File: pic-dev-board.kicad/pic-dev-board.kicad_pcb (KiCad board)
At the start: 2 copper layers, 100 x 100 mm, 78 parts, among them J1 Conn_GP0, J10 Jumper DATin, J11 Conn_SR_2, J12 Conn_SR_1, J13 Conn_5V_GND, J14 Jumper CLKin, J15 Barrel_Jack_Switch, J16 RUN/~PGM, J17 I2C, J18 GP1(RA1)/RB6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

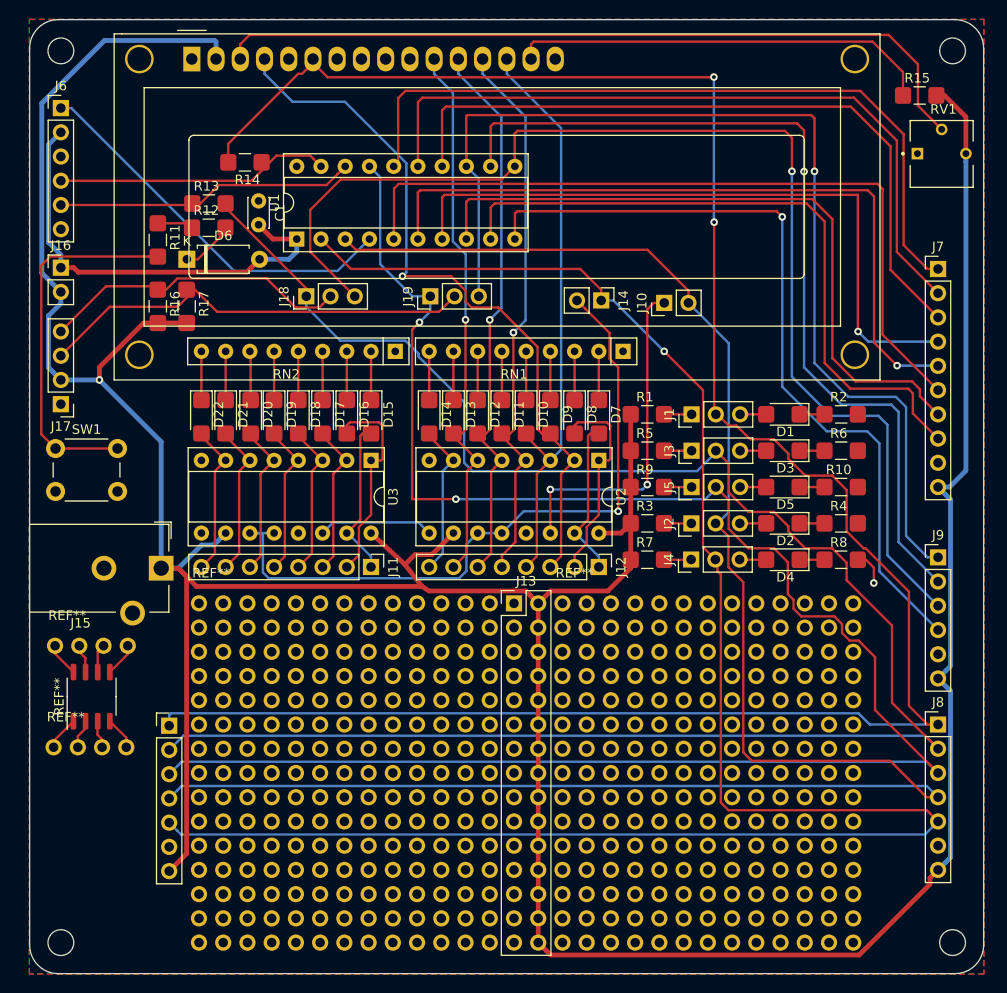
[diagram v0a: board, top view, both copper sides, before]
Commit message: added labels
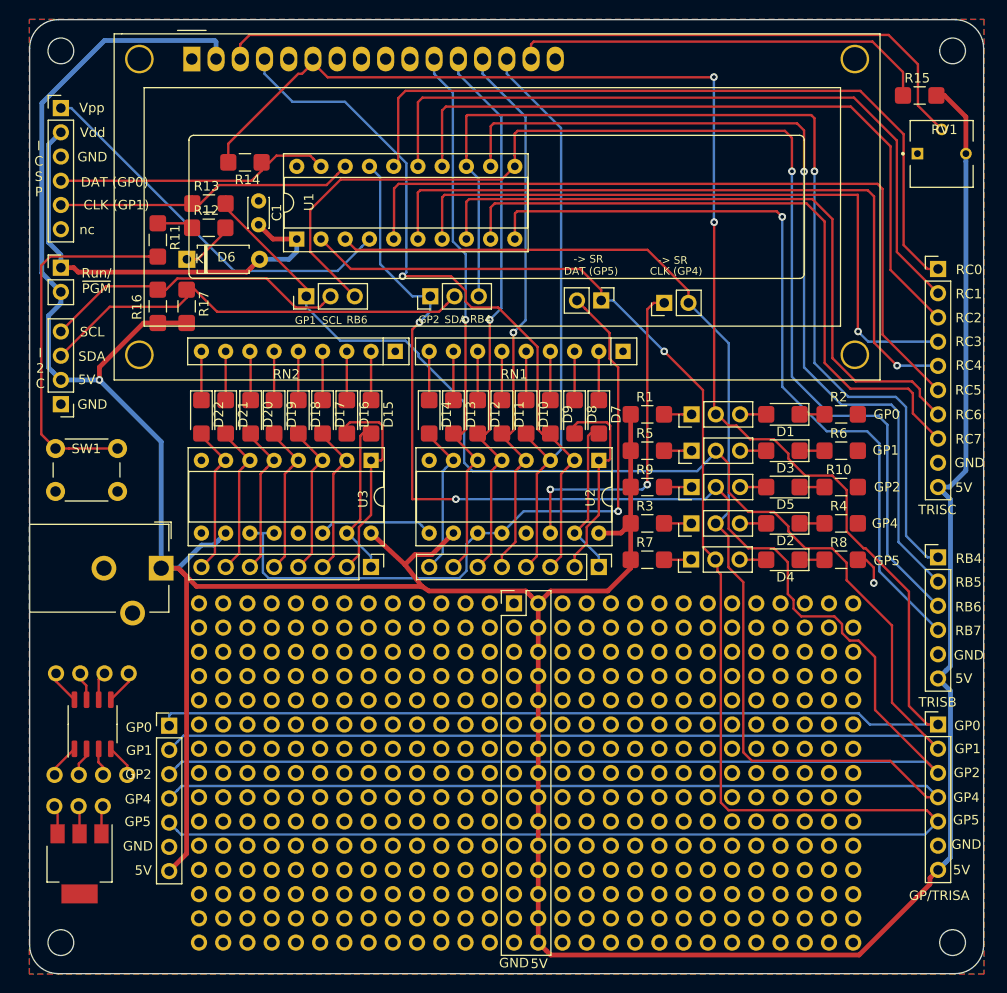
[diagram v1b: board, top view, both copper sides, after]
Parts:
- removed the REF** at (32.5, 106.3)
- removed the REF** at (32.7, 95.6)
- added REF**: Proto_Area_03x01_P2.54mm_Drill1.0mm, Proto_Area:Proto_Area_03x01, F.Cu at (37.7, 112.4)
- added REF**: SOT-223, Package_TO_SOT_SMD:SOT-223, F.Cu at (35.2, 118.5)
- added REF**: Proto_Area_04x01_P2.54mm_Drill1.0mm, Proto_Area:Proto_Area_04x01, F.Cu at (32.6, 109.2)
- added REF**: Proto_Area_04x01_P2.54mm_Drill1.0mm, Proto_Area:Proto_Area_04x01, F.Cu at (32.8, 98.5)
- moved REF** 2.90 mm to (36.6, 103.9)
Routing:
- net (no net): track 26.2 -> 35.1 mm
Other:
- board text added: "-> SR"
- board text added: "5V"
- board text added: "CLK (GP1)"
- board text added: "CLK (GP4)"
- board text added: "DAT (GP0)"
- board text added: "DAT (GP5)"
- board text added: "GND"
- board text added: "GP/TRISA"
- board text added: "GP0"
- board text added: "GP1"
- board text added: "GP2"
- board text added: "GP4"
- board text added: "GP5"
- board text added: "I 2 C"
- board text added: "I C S P"
- board text added: "RB4"
- board text added: "RB5"
- board text added: "RB6"
- board text added: "RB7"
- board text added: "RC0"
- board text added: "RC1"
- board text added: "RC2"
- board text added: "RC3"
- board text added: "RC4"
- board text added: "RC5"
- board text added: "RC6"
- board text added: "RC7"
- board text added: "Run/ ~PGM"
- board text added: "SCL"
- board text added: "SDA"
- board text added: "TRISB"
- board text added: "TRISC"
- board text added: "Vdd"
- board text added: "Vpp"
- board text added: "nc"

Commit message: Rev1: updated date/revision and added label
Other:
- board text added: "Rev 1"
- board text added: "https://github.com/bablokb/pcb-pic-devboard"
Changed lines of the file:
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@@
   (general
     (thickness 1.6)
-    (drawings 71)
+    (drawings 73)
     (tracks 699)
     (zones 0)
@@
     )
   )
+  (gr_text "Rev 1" (at 112.4458 39.9796) (layer B.SilkS)
+    (effects (font (size 1 1) (thickness 0.15)) (justify mirror))
+  )
+  (gr_text https://github.com/bablokb/pcb-pic-devboard (at 96.2152 38.3286) (layer B.SilkS)
+    (effects (font (size 1 1) (thickness 0.15)) (justify mirror))
+  )
   (gr_text GP4 (at 119.6594 82.804) (layer F.SilkS)
     (effects (font (size 1 1) (thickness 0.15)))
@@
   )
   (gr_text 5V (at 127.9144 79.0448) (layer F.SilkS)
-    (effects (font (size 1 1) (thickness 0.15)))
+    (effects (font (size 1 0.8) (thickness 0.15)))
   )
-  (gr_text GND (at 128.524 76.454) (layer F.SilkS)
-    (effects (font (size 1 1) (thickness 0.15)))
+  (gr_text GND (at 128.2954 76.4286) (layer F.SilkS)
+    (effects (font (size 1 0.8) (thickness 0.15)))
   )
-  (gr_text RC7 (at 128.4224 73.9648) (layer F.SilkS)
-    (effects (font (size 1 1) (thickness 0.15)))
+  (gr_text RC7 (at 128.1938 73.9394) (layer F.SilkS)
+    (effects (font (size 1 0.8) (thickness 0.15)))
   )
-  (gr_text RC6 (at 128.4224 71.4248) (layer F.SilkS)
-    (effects (font (size 1 1) (thickness 0.15)))
+  (gr_text RC6 (at 128.1938 71.3994) (layer F.SilkS)
+    (effects (font (size 1 0.8) (thickness 0.15)))
   )
-  (gr_text RC5 (at 128.397 68.834) (layer F.SilkS)
-    (effects (font (size 1 1) (thickness 0.15)))
+  (gr_text RC5 (at 128.1684 68.8086) (layer F.SilkS)
+    (effects (font (size 1 0.8) (thickness 0.15)))
   )
-  (gr_text RC4 (at 128.4478 66.2432) (layer F.SilkS)
-    (effects (font (size 1 1) (thickness 0.15)))
+  (gr_text RC4 (at 128.2192 66.2178) (layer F.SilkS)
+    (effects (font (size 1 0.8) (thickness 0.15)))
   )
-  (gr_text RC3 (at 128.4224 63.754) (layer F.SilkS)
-    (effects (font (size 1 1) (thickness 0.15)))
+  (gr_text RC3 (at 128.1938 63.7286) (layer F.SilkS)
+    (effects (font (size 1 0.8) (thickness 0.15)))
   )
-  (gr_text RC2 (at 128.4224 61.2648) (layer F.SilkS)
-    (effects (font (size 1 1) (thickness 0.15)))
+  (gr_text RC2 (at 128.1938 61.2394) (layer F.SilkS)
+    (effects (font (size 1 0.8) (thickness 0.15)))
   )
-  (gr_text RC1 (at 128.4478 58.7502) (layer F.SilkS)
-    (effects (font (size 1 1) (thickness 0.15)))
+  (gr_text RC1 (at 128.2192 58.7248) (layer F.SilkS)
+    (effects (font (size 1 0.8) (thickness 0.15)))
   )
-  (gr_text RC0 (at 128.4732 56.2102) (layer F.SilkS)
-    (effects (font (size 1 1) (thickness 0.15)))
+  (gr_text RC0 (at 128.2446 56.1848) (layer F.SilkS)
+    (effects (font (size 1 0.8) (thickness 0.15)))
   )
-  (gr_text 5V (at 127.9144 99.06) (layer F.SilkS)
-    (effects (font (size 1 1) (thickness 0.15)))
+  (gr_text 5V (at 127.7874 99.0346) (layer F.SilkS)
+    (effects (font (size 1 0.8) (thickness 0.15)))
   )
-  (gr_text GND (at 128.4478 96.6216) (layer F.SilkS)
-    (effects (font (size 1 1) (thickness 0.15)))
+  (gr_text GND (at 128.3208 96.5962) (layer F.SilkS)
+    (effects (font (size 1 0.8) (thickness 0.15)))
   )
-  (gr_text RB7 (at 128.397 94.0562) (layer F.SilkS)
-    (effects (font (size 1 1) (thickness 0.15)))
+  (gr_text RB7 (at 128.27 94.0308) (layer F.SilkS)
+    (effects (font (size 1 0.8) (thickness 0.15)))
   )
-  (gr_text RB6 (at 128.397 91.567) (layer F.SilkS)
-    (effects (font (size 1 1) (thickness 0.15)))
+  (gr_text RB6 (at 128.27 91.5416) (layer F.SilkS)
+    (effects (font (size 1 0.8) (thickness 0.15)))
   )
-  (gr_text RB5 (at 128.4224 88.9762) (layer F.SilkS)
-    (effects (font (size 1 1) (thickness 0.15)))
+  (gr_text RB5 (at 128.2954 88.9508) (layer F.SilkS)
+    (effects (font (size 1 0.8) (thickness 0.15)))
   )
-  (gr_text RB4 (at 128.4478 86.487) (layer F.SilkS)
-    (effects (font (size 1 1) (thickness 0.15)))
+  (gr_text RB4 (at 128.3208 86.4616) (layer F.SilkS)
+    (effects (font (size 1 0.8) (thickness 0.15)))
   )
   (gr_text TRISC (at 125.1458 81.3816) (layer F.SilkS)
@@
   )
   (gr_text 5V (at 127.6858 119.126) (layer F.SilkS)
-    (effects (font (size 1 1) (thickness 0.15)))
+    (effects (font (size 1 0.8) (thickness 0.15)))
   )
   (gr_text GP1 (at 128.3208 106.426) (layer F.SilkS)
-    (effects (font (size 1 1) (thickness 0.15)))
+    (effects (font (size 1 0.8) (thickness 0.15)))
   )
   (gr_text GP2 (at 128.2446 108.9406) (layer F.SilkS)
-    (effects (font (size 1 1) (thickness 0.15)))
+    (effects (font (size 1 0.8) (thickness 0.15)))
   )
   (gr_text GP5 (at 128.1684 113.8936) (layer F.SilkS)
-    (effects (font (size 1 1) (thickness 0.15)))
+    (effects (font (size 1 0.8) (thickness 0.15)))
   )
   (gr_text GP0 (at 128.2954 104.013) (layer F.SilkS)
-    (effects (font (size 1 1) (thickness 0.15)))
+    (effects (font (size 1 0.8) (thickness 0.15)))
   )
   (gr_text GND (at 128.1938 116.459) (layer F.SilkS)
-    (effects (font (size 1 1) (thickness 0.15)))
+    (effects (font (size 1 0.8) (thickness 0.15)))
   )
   (gr_text GP4 (at 128.1938 111.5314) (layer F.SilkS)
-    (effects (font (size 1 1) (thickness 0.15)))
+    (effects (font (size 1 0.8) (thickness 0.15)))
   )
   (gr_text 5V (at 83.4136 128.9558) (layer F.SilkS)

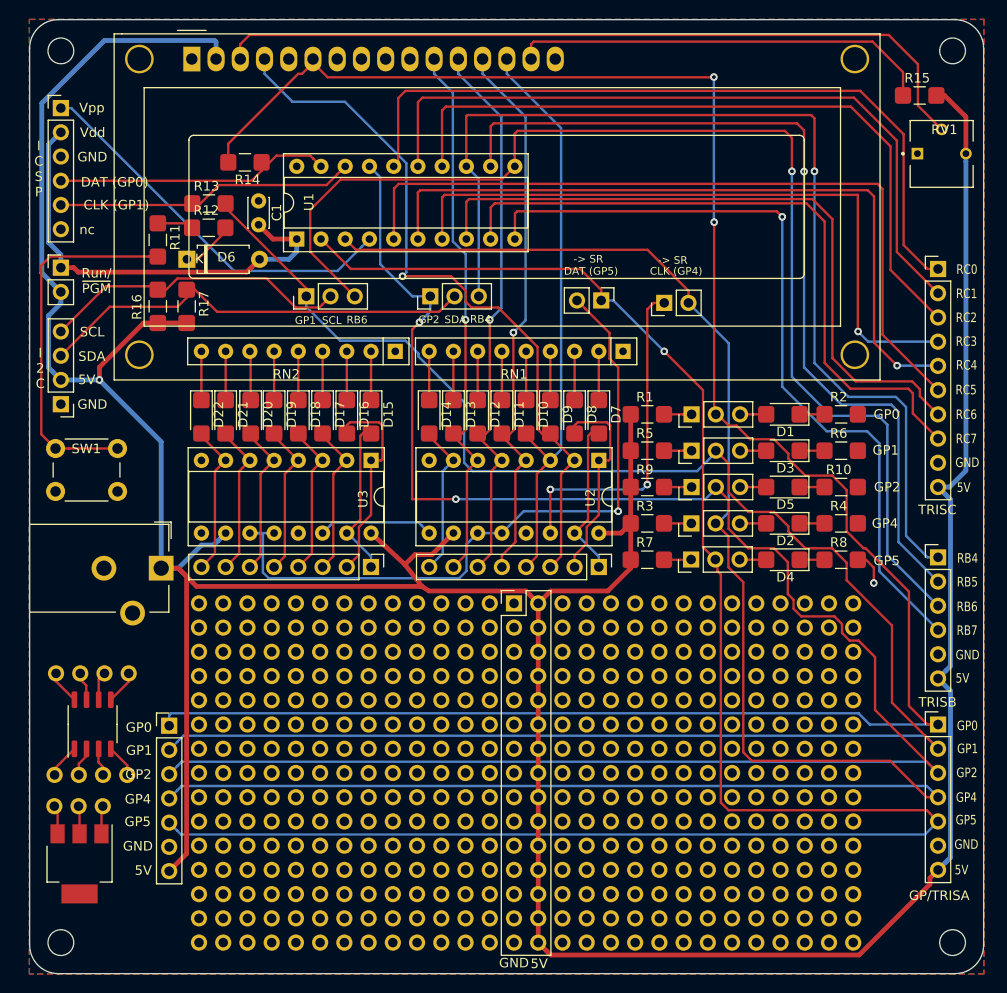
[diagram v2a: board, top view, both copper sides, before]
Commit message: updated to new I2C-layout
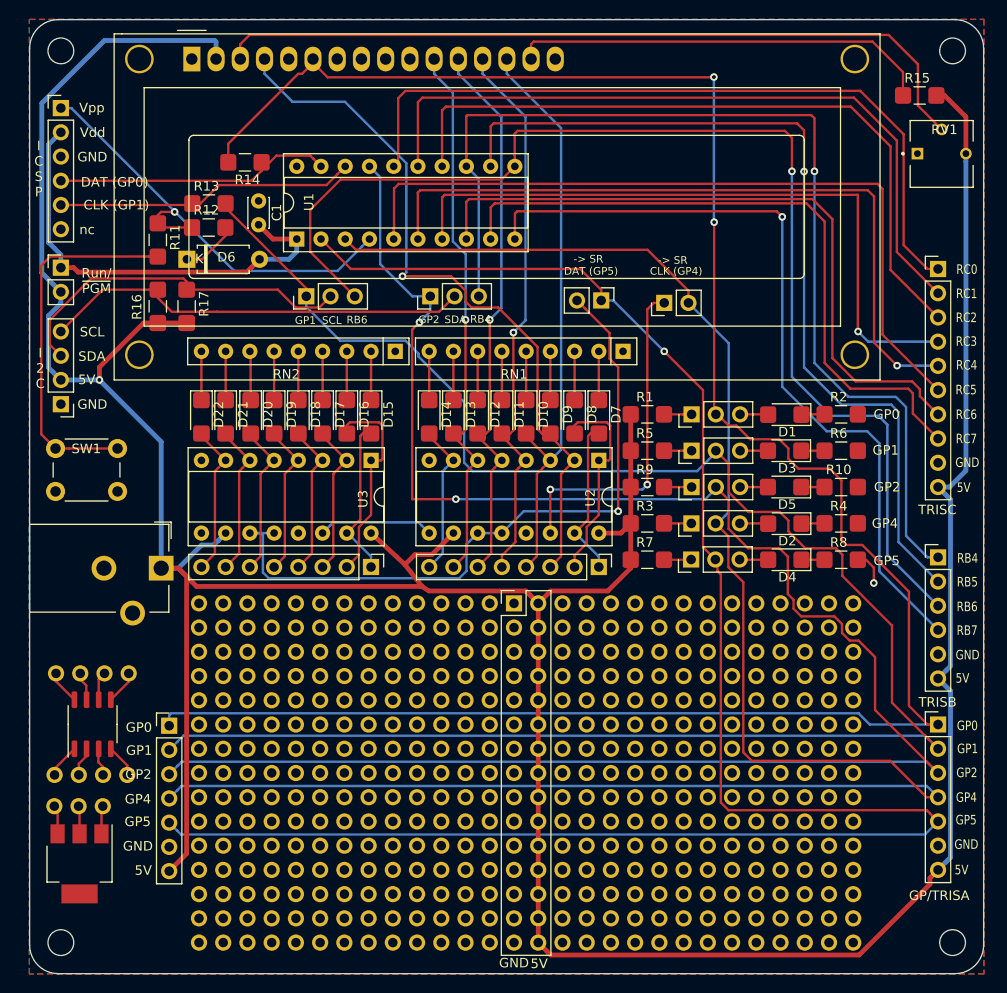
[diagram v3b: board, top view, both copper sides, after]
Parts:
- moved D1 0.20 mm to (109.4, 71.4)
- moved D2 0.20 mm to (109.4, 82.8)
- moved D4 0.20 mm to (109.4, 86.6)
- moved D3 0.18 mm to (109.4, 75.2)
- moved D5 0.18 mm to (109.4, 79.0)
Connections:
- J17 pad 3: /SDA -> /SCL
- J17 pad 4: /SCL -> /SDA
- R11 pad 1: Net-(R11-Pad1) -> Net-(J6-Pad1)
- R12 pad 1: Net-(R11-Pad1) -> Net-(J6-Pad1)
- R16 pad 1: /SCL -> /SDA
- R17 pad 1: /SDA -> /SCL
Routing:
- net Net-(J6-Pad1): track 40.8 -> 48.8 mm, vias 0 -> 1
- net /SCL: track 32.3 -> 38.6 mm
- net Net-(R11-Pad1): track 3.79 -> 0.00 mm
- net /SDA: track 47.1 -> 45.2 mm
- net /GP0: track 222.0 -> 223.5 mm
- net /GP1: track 196.4 -> 197.0 mm

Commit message: updated revision label
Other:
- board text added: "Rev 2"
- board text removed: "Rev 1"

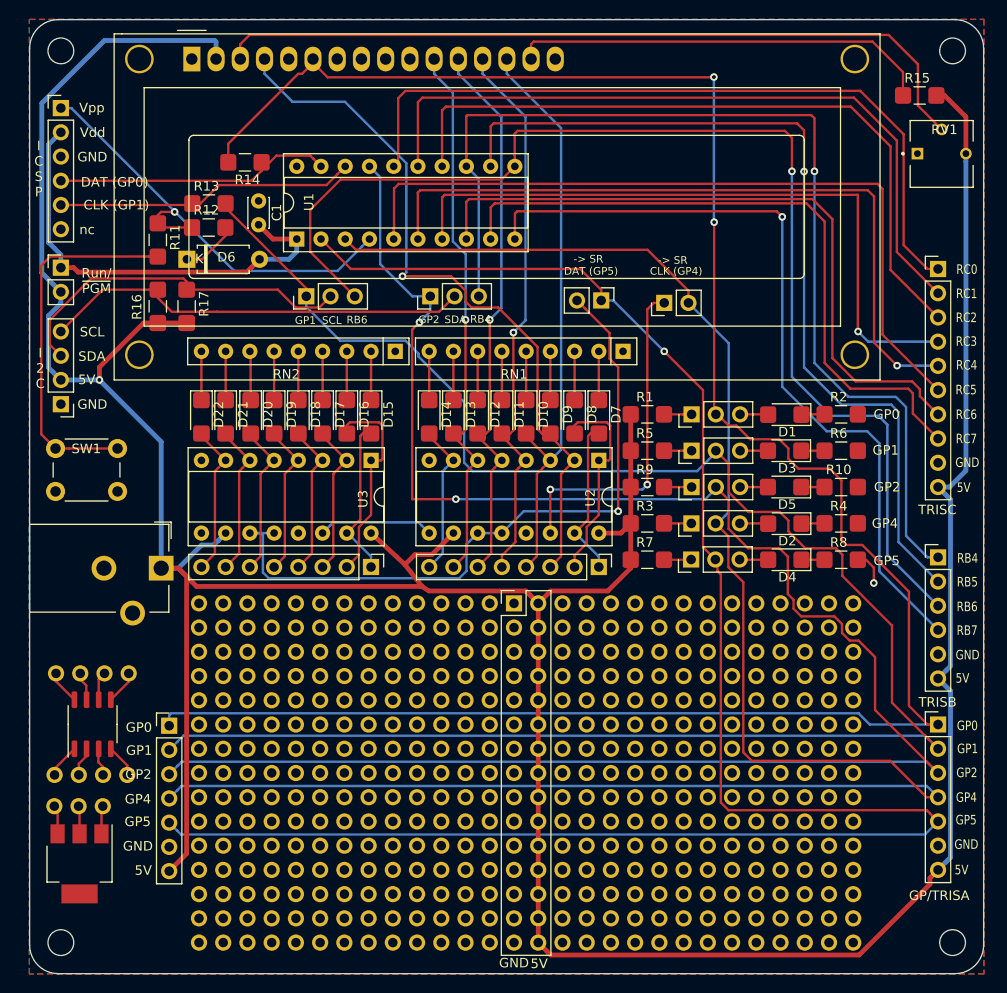
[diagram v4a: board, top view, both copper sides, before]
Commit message: layout with textool
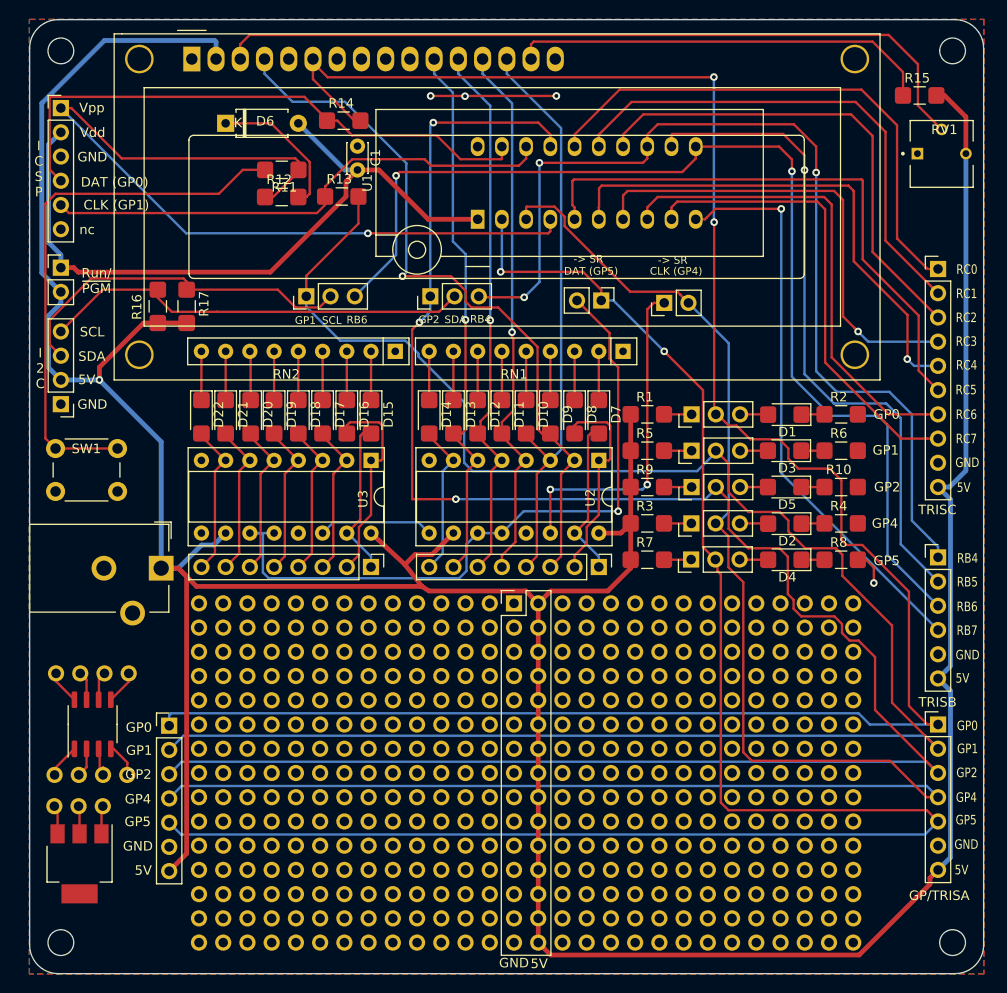
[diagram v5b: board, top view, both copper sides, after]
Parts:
- U1: footprint Package_DIP:DIP-20_W7.62mm_Socket -> Socket:DIP_Socket-20_W4.3_W5.08_W7.62_W10.16_W10.9_3M_220-3342-00-0602J
- moved U1 19.1 mm to (77.0, 50.9)
- moved R11 15.0 mm to (56.7, 45.7), turned to 180 degrees
- moved D6 14.8 mm to (50.5, 40.9)
- moved R13 13.9 mm to (62.5, 48.5)
- moved C1 11.8 mm to (64.4, 43.3)
- moved R14 10.8 mm to (62.7, 40.6), turned to 0 degrees
- moved R12 8.29 mm to (56.2, 48.6)
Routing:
- net Net-(J6-Pad1): track 48.8 -> 91.0 mm
- net Net-(J6-Pad4): track 29.3 -> 60.6 mm
- net /Vdd: track 47.0 -> 74.9 mm
- net /RB5: track 93.7 -> 69.8 mm
- net /RC2: track 74.8 -> 51.1 mm
- net /RC1: track 76.8 -> 53.2 mm
- net /RB7: track 83.6 -> 60.4 mm
- net /RC0: track 78.8 -> 56.0 mm
- net /RC4: track 76.1 -> 53.8 mm
- net Net-(J6-Pad5): track 32.3 -> 54.4 mm
- net /RC3: track 71.2 -> 49.4 mm
- net /RC7: track 70.5 -> 49.1 mm
- net /RC6: track 71.8 -> 51.0 mm
- net /RC5: track 80.4 -> 59.9 mm
- net Net-(R11-Pad2): track 38.9 -> 57.1 mm
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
